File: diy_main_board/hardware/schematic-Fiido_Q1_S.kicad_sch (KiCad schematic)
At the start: 6 parts, among them J1 Connector_3, J2 Connector_1, U1 ESP32-S3-DevKitC

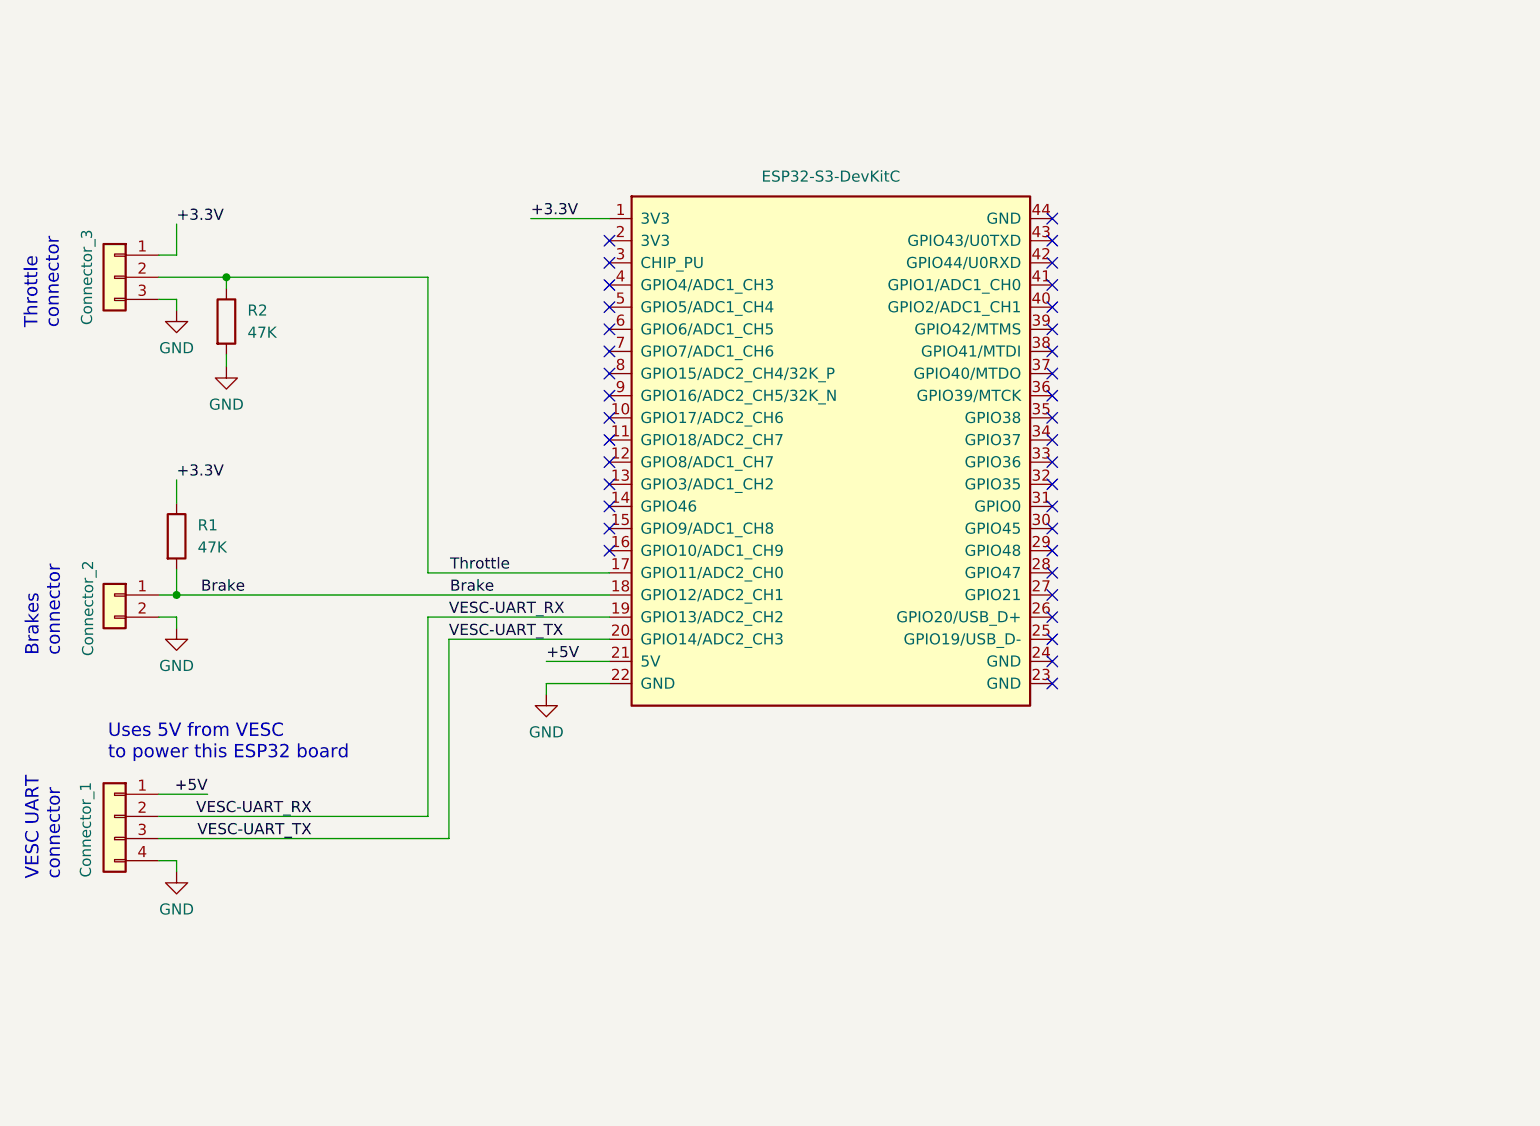
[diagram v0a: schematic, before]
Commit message: Added low pass filter to filter out the throttle false signals / noise
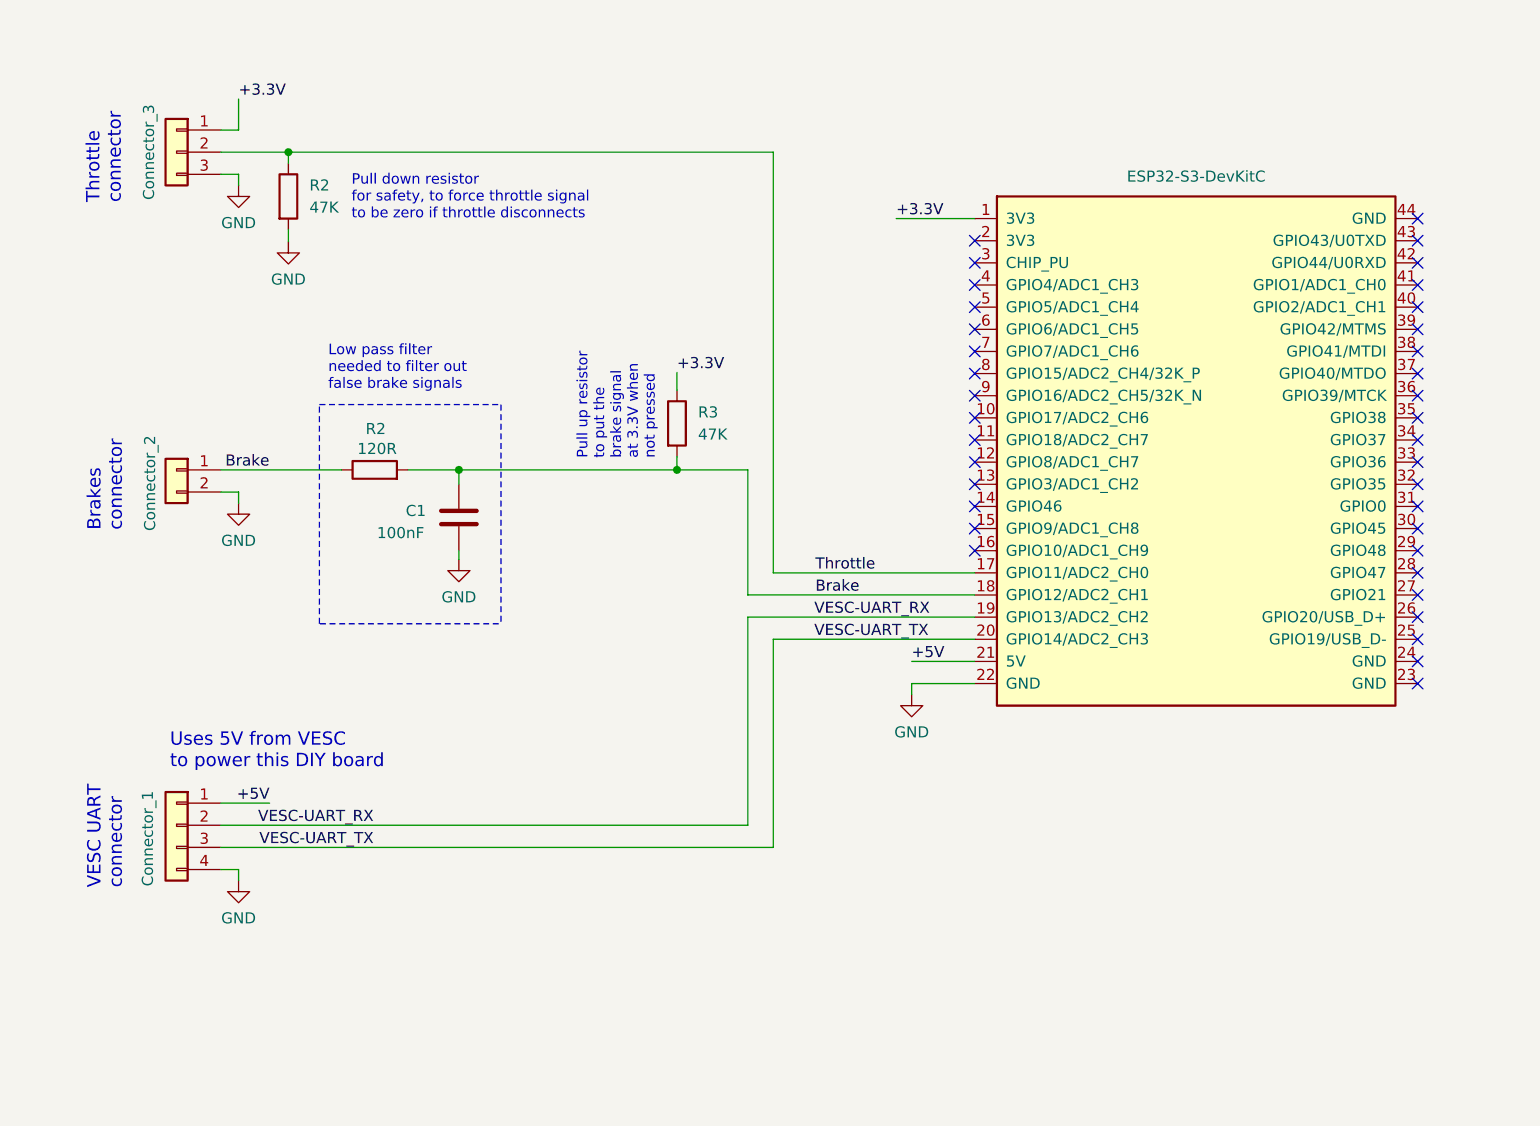
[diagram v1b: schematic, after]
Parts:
- added C1: 100nF, symbol Device:C
- added R2: 120R, symbol Device:R
- renumbered R1 to R3
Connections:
- net Brake: now also C1.1, R2.1, R2.2
- net GND: now also C1.2
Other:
- note added: "Low pass filter needed to filter out false brake signals"
- note added: "Pull down resistor for safety, to force throttle signal to be zero if throttle disconnects"
- note added: "Pull up resistor to put the brake signal at 3.3V when not pressed"
- note added: "Uses 5V from VESC to power this DIY board"
- note removed: "Uses 5V from VESC to power this ESP32 board"
- moved on the sheet: Connector_2, R2, R3

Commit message: Added DC-DC to power the main board and avoid noise from the 5V line of VESC
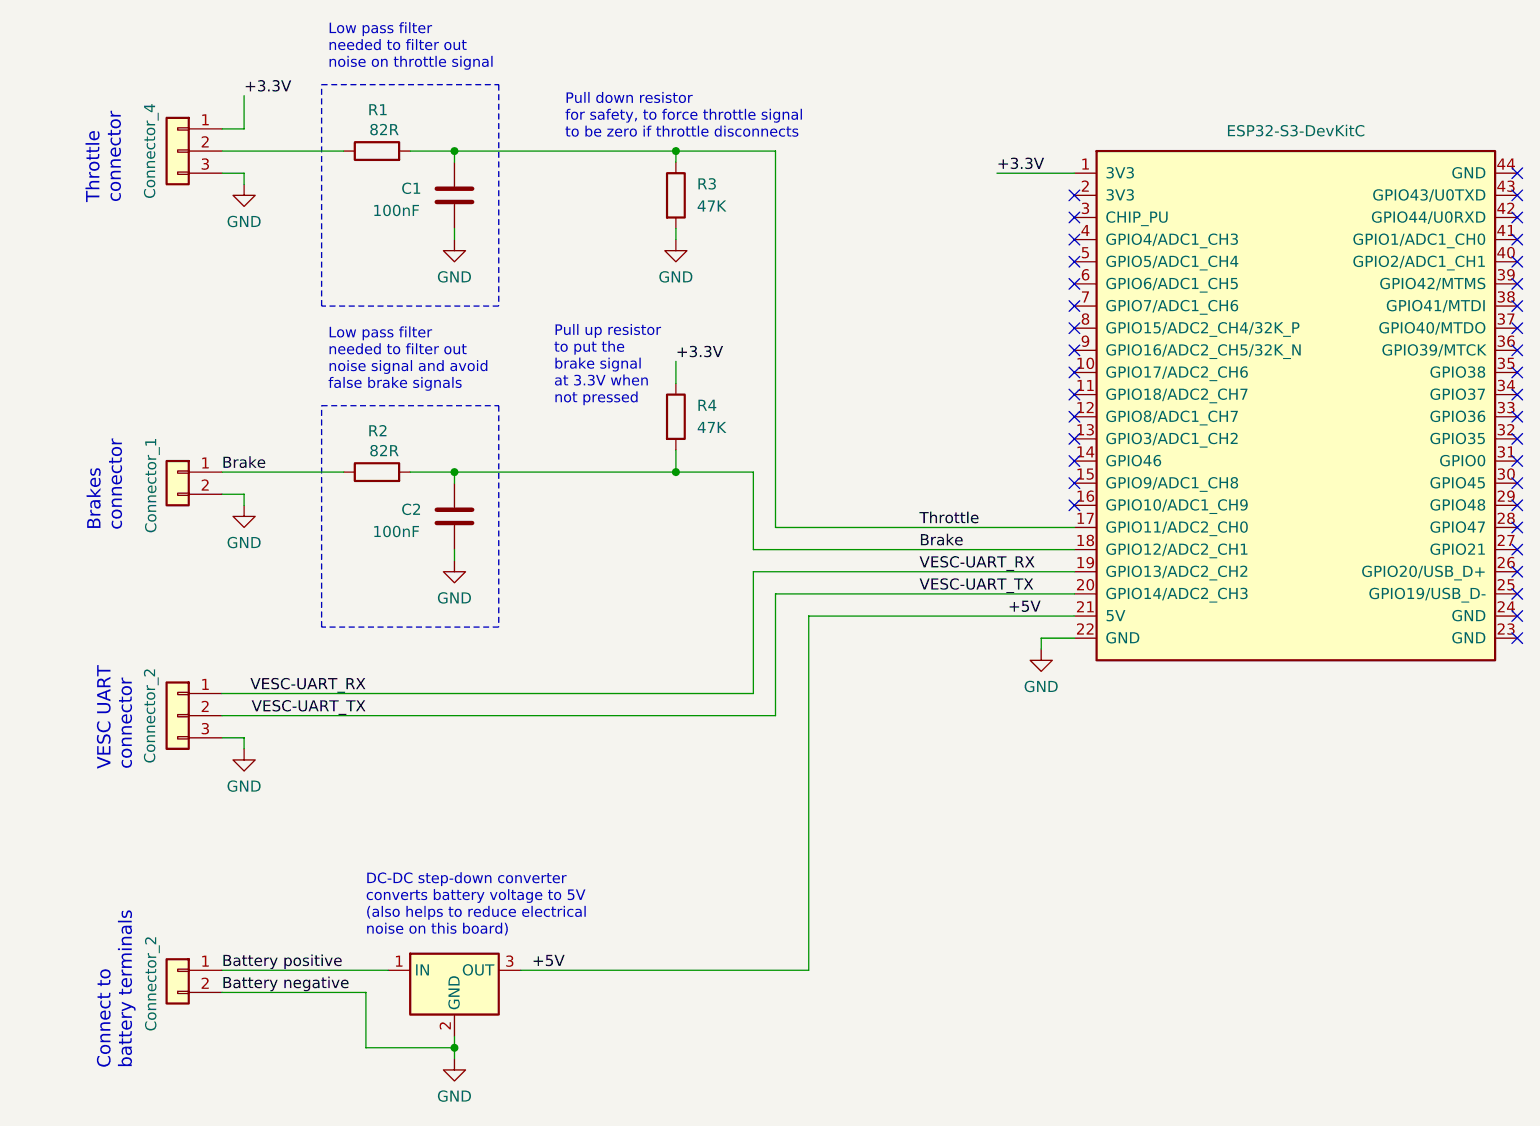
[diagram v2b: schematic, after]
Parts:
- removed J2: Connector_1, symbol Connector_Generic:Conn_01x04
- added C1: 100nF, symbol Device:C
- added Connector_2: ~, symbol Connector_Generic:Conn_01x02
- added J2: Connector_2, symbol Connector_Generic:Conn_01x03
- added R1: 82R, symbol Device:R
- added U1: Step-down converter to 3.3V, Converter_DCDC:Converter_DCDC_Murata_OKI-78SR_Vertical, symbol Converter_DCDC:OKI-78SR-3.3_1.5-W36-C
- J1: value Connector_3 -> Connector_4
- R2: value 120R -> 82R
- renumbered C1 to C2, Connector_2 to Connector_1, R2 to R3, R3 to R4, U1 to U2
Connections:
- net +5V: now also U1.3 (OUT)
- net GND: now also C1.2, Connector_2.2 (Pin_2), J2.3 (Pin_3), U1.2 (GND)
- net Throttle: now also C1.1, R1.2; no longer J1.2 (Pin_2)
- net VESC-UART_RX: now also J2.1 (Pin_1)
- net VESC-UART_TX: now also J2.2 (Pin_2)
- new net: J1.2 (Pin_2), R1.1
- new net Battery positive: Connector_2.1 (Pin_1), U1.1 (IN)
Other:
- note added: "Connect to battery terminals"
- note added: "DC-DC step-down converter converts battery voltage to 5V (also helps to reduce electrical noise on this board)"
- note added: "Low pass filter needed to filter out noise on throttle signal"
- note added: "Low pass filter needed to filter out noise signal and avoid false brake signals"
- note removed: "Low pass filter needed to filter out false brake signals"
- note removed: "Uses 5V from VESC to power this DIY board"
- moved on the sheet: C2, R3, R4
